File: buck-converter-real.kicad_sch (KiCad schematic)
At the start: 118 parts, among them J1 USB_C_2.0_16P, J10 I2C1, J14 Conn_01x04, J15 Conn_01x06, J2 U.FL, J3 MSD-1-A, J4 POWER, J7 Conn_01x06 2.54mm Screw Termi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, J8 I2C1, J9 SWD, Q10 NTTFS5C680NL, Q8 DMT6030LFCL-7, Q9 NTTFS5C680NL, SW1 WIO_RST, SW2 SW, SW3 SW, U1 MIC4605, U10 TLV75733PDRV 3V3@1A, U11 TPS613222ADBV, U12 INA180A1, U13 TPS22991CRAAR, U2 LM66200DRLR, U4 LV2862XDDC, U6 TPT482-VS2R, U7 TPS22991CRAAR, U8 LM66200DRLR, Y2 Crystal_GND2

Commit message: All routed
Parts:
- removed D13: E1J, Diode_SMD:D_SOD-123F, symbol PCM_Diode_Schottky_AKL:SS56
- removed Q8: DMT6030LFCL-7, buck-forest:DMT6030LFCL-7, symbol buck-wio:DMT6030LFCL-7

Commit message: Swap clamp diode to lower voltage.
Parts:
- added R52, R53: 1M, Resistor_SMD:R_0603_1608Metric_Pad0.98x0.95mm_HandSolder, symbol Device:R_US
- D4: value SMBJ54A -> SMBJ36A
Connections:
- net GND: now also R52.2, R53.2
- net at R47.2, U1.8 (LO): now also R53.1
- net at R48.2, U1.3 (HO): now also R52.1

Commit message: Add details to schematic
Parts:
- TP2: footprint (none) -> TestPoint:TestPoint_Keystone_5015_Micro_Mini
- U1: value MIC4605 -> MIC4605-2YM
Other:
- note added: "3V3 ~10mA MAX"
- note added: "3V3 ~160mA MAX"
- note added: "3V3 ~600mA budget"
- note added: "@ ~200mAnom load"
- note added: "USB Interface (Device/Host)"
- note added: "WIO I2C"
- note removed: "@ 400 mAnom"
- note removed: "USB Interface"
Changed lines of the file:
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@@
 	(text "Ideal diode (OR)"
 		(exclude_from_sim no)
-		(at 216.662 221.234 0)
+		(at 215.9 218.694 0)
 		(effects
 			(font
@@
 	(text "USB"
 		(exclude_from_sim no)
-		(at 131.826 281.686 0)
+		(at 132.588 285.75 0)
 		(effects
 			(font
@@
 		)
 	)
+	(text "3V3 ~600mA budget"
+		(exclude_from_sim no)
+		(at 676.656 314.96 0)
+		(effects
+			(font
+				(size 1.27 1.27)
+			)
+		)
+	)
 	(text "USB 5V out switch"
 		(exclude_from_sim no)
@@
 		)
 	)
-	(text "USB Interface"
+	(text "USB Interface\n(Device/Host)"
 		(exclude_from_sim no)
 		(at 360.934 279.654 0)
@@
 		)
 	)
+	(text "3V3 ~10mA MAX"
+		(exclude_from_sim no)
+		(at 625.348 169.418 0)
+		(effects
+			(font
+				(size 1.27 1.27)
+			)
+		)
+	)
+	(text "WIO I2C"
+		(exclude_from_sim no)
+		(at 676.656 311.658 0)
+		(effects
+			(font
+				(size 2.54 2.54)
+				(thickness 0.508)
+				(bold yes)
+			)
+		)
+	)
 	(text "Active Low"
 		(exclude_from_sim no)
@@
 		)
 	)
+	(text "3V3 ~160mA MAX"
+		(exclude_from_sim no)
+		(at 546.608 218.948 0)
+		(effects
+			(font
+				(size 1.27 1.27)
+			)
+		)
+	)
 	(text "WIO SWD"
 		(exclude_from_sim no)
@@
 		)
 	)
-	(text "@ 400 mAnom"
+	(text "@ ~200mAnom load"
 		(exclude_from_sim no)
-		(at 182.118 168.148 0)
+		(at 173.736 165.1 0)
 		(effects
 			(font
@@
 		(dnp no)
 		(property "Reference" "J1"
-			(at 126.492 301.498 0)
+			(at 130.81 301.498 0)
 			(show_name no)
 			(do_not_autoplace no)
@@
 		)
 		(property "Value" "USB_C_2.0_16P"
-			(at 126.492 304.038 0)
+			(at 130.81 304.038 0)
 			(show_name no)
 			(do_not_autoplace no)
@@
 		(dnp no)
 		(property "Reference" "U13"
-			(at 42.926 233.172 0)
+			(at 43.18 230.886 0)
 			(show_name no)
 			(do_not_autoplace no)
@@
 		)
 		(property "Value" "TPS22991CRAAR"
-			(at 42.926 235.712 0)
+			(at 43.18 233.426 0)
 			(show_name no)
 			(do_not_autoplace no)
@@
 			)
 		)
-		(property "Description" ""
-			(at 43.18 243.84 0)
-			(hide yes)
+		(property "Description" "2A Max Cont."
+			(at 43.434 235.458 0)
 			(show_name no)
 			(do_not_autoplace no)
@@
 			)
 		)
-		(property "Footprint" ""
+		(property "Footprint" "TestPoint:TestPoint_Keystone_5015_Micro_Mini"
 			(at 182.88 208.28 0)
 			(hide yes)
@@
 		(dnp no)
 		(property "Reference" "U2"
-			(at 215.9 226.06 0)
+			(at 215.9 223.266 0)
 			(show_name no)
 			(do_not_autoplace no)
@@
 		)
 		(property "Value" "LM66200DRLR"
-			(at 215.9 228.346 0)
+			(at 215.9 225.552 0)
 			(show_name no)
 			(do_not_autoplace no)
@@
 			)
 		)
-		(property "Description" ""
-			(at 215.9 238.76 0)
-			(hide yes)
+		(property "Description" "2.5A Cont."
+			(at 215.9 227.584 0)
 			(show_name no)
 			(do_not_autoplace no)
@@
 		(dnp no)
 		(property "Reference" "U7"
-			(at 182.626 253.492 0)
+			(at 182.88 251.206 0)
 			(show_name no)
 			(do_not_autoplace no)
@@
 		)
 		(property "Value" "TPS22991CRAAR"
-			(at 182.626 256.032 0)
+			(at 182.88 253.746 0)
 			(show_name no)
 			(do_not_autoplace no)
@@
 			)
 		)
-		(property "Description" ""
-			(at 182.88 264.16 0)
-			(hide yes)
+		(property "Description" "2A Max Cont."
+			(at 182.88 256.286 0)
 			(show_name no)
 			(do_not_autoplace no)
@@
 		(in_pos_files yes)
 		(dnp no)
-		(fields_autoplaced yes)
 		(property "Reference" "U1"
-			(at 284.2795 111.76 0)
+			(at 272.288 111.252 0)
 			(show_name no)
 			(do_not_autoplace no)
@@
 			)
 		)
-		(property "Value" "MIC4605"
-			(at 284.2795 114.3 0)
+		(property "Value" "MIC4605-2YM"
+			(at 267.208 114.046 0)
 			(show_name no)
 			(do_not_autoplace no)

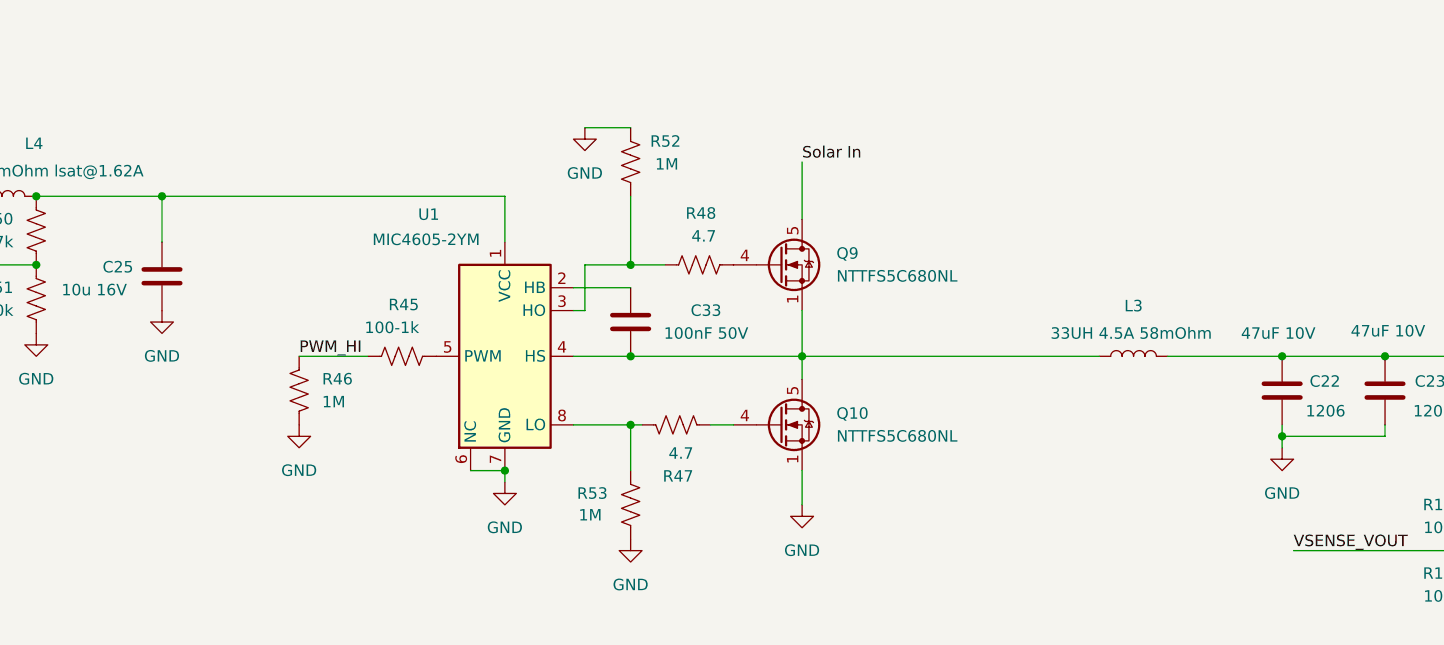
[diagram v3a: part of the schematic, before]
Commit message: Add test point footprint and pads.
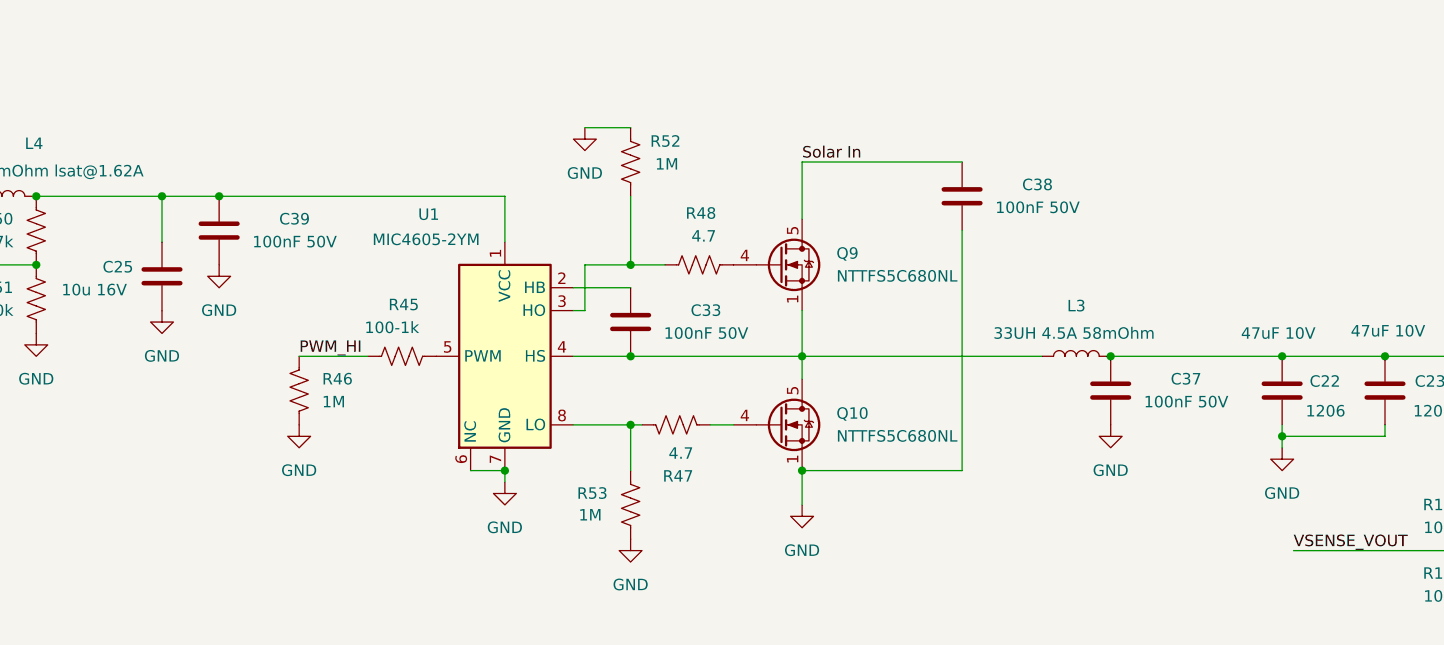
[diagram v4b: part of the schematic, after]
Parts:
- added C37, C38, C39: 100nF 50V, Capacitor_SMD:C_0603_1608Metric_Pad1.08x0.95mm_HandSolder, symbol PCM_Capacitor_AKL:C_0805
- TP1: footprint (none) -> buck-forest:Testpad
- TP2: footprint TestPoint:TestPoint_Keystone_5015_Micro_Mini -> buck-forest:Testpad
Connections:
- net GND: now also C37.1, C38.1, C39.1
- net Solar In: now also C38.2
- net at C25.1, L4.2, R50.1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: now also C39.2
- net at C22.1, C23.1, F1.1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: now also C37.2
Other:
- moved on the sheet: L3

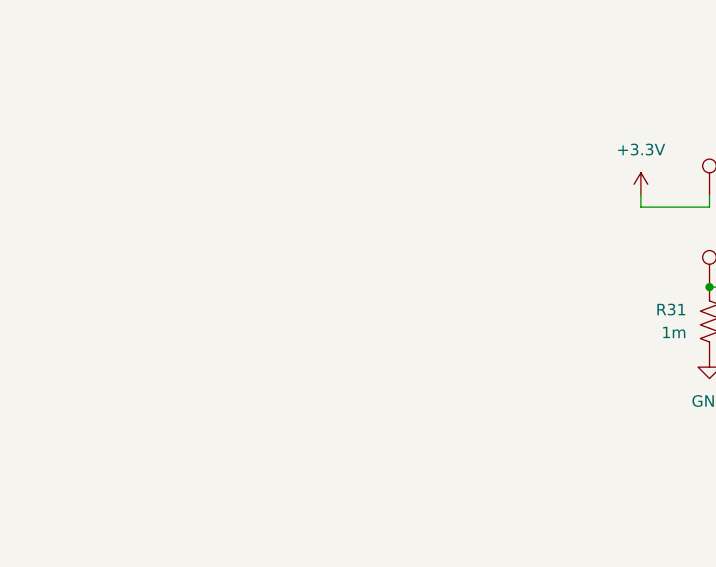
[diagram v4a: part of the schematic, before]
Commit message: Add test holes. More to come
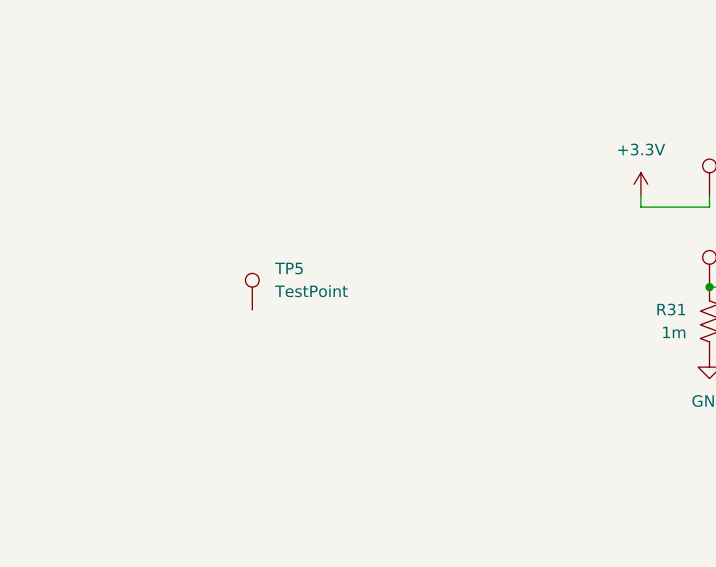
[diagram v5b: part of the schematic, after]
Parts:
- added TP5: TestPoint, buck-forest:Testhole, symbol Connector:TestPoint
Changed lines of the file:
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@@
+	)
+	(symbol
+		(lib_id "Connector:TestPoint")
+		(at 39.37 172.72 0)
+		(unit 1)
+		(body_style 1)
+		(exclude_from_sim no)
+		(in_bom yes)
+		(on_board yes)
+		(in_pos_files yes)
+		(dnp no)
+		(fields_autoplaced yes)
+		(property "Reference" "TP5"
+			(at 41.91 168.1479 0)
+			(show_name no)
+			(do_not_autoplace no)
+			(effects
+				(font
+					(size 1.27 1.27)
+				)
+				(justify left)
+			)
+		)
+		(property "Value" "TestPoint"
+			(at 41.91 170.6879 0)
+			(show_name no)
+			(do_not_autoplace no)
+			(effects
+				(font
+					(size 1.27 1.27)
+				)
+				(justify left)
+			)
+		)
+		(property "Footprint" "buck-forest:Testhole"
+			(at 44.45 172.72 0)
+			(hide yes)
+			(show_name no)
+			(do_not_autoplace no)
+			(effects
+				(font
+					(size 1.27 1.27)
+				)
+			)
+		)
+		(property "Datasheet" ""
+			(at 44.45 172.72 0)
+			(hide yes)
+			(show_name no)
+			(do_not_autoplace no)
+			(effects
+				(font
+					(size 1.27 1.27)
+				)
+			)
+		)
+		(property "Description" "test point"
+			(at 39.37 172.72 0)
+			(hide yes)
+			(show_name no)
+			(do_not_autoplace no)
+			(effects
+				(font
+					(size 1.27 1.27)
+				)
+			)
+		)
+		(pin "1"
+		)
+		(instances
+			(project "buck-converter-real"
+				(path "/cbc98a1b-0533-4e8d-81af-0515d3e50555"
+					(reference "TP5")
+					(unit 1)
+				)
+			)
+		)
 	)
 	(symbol

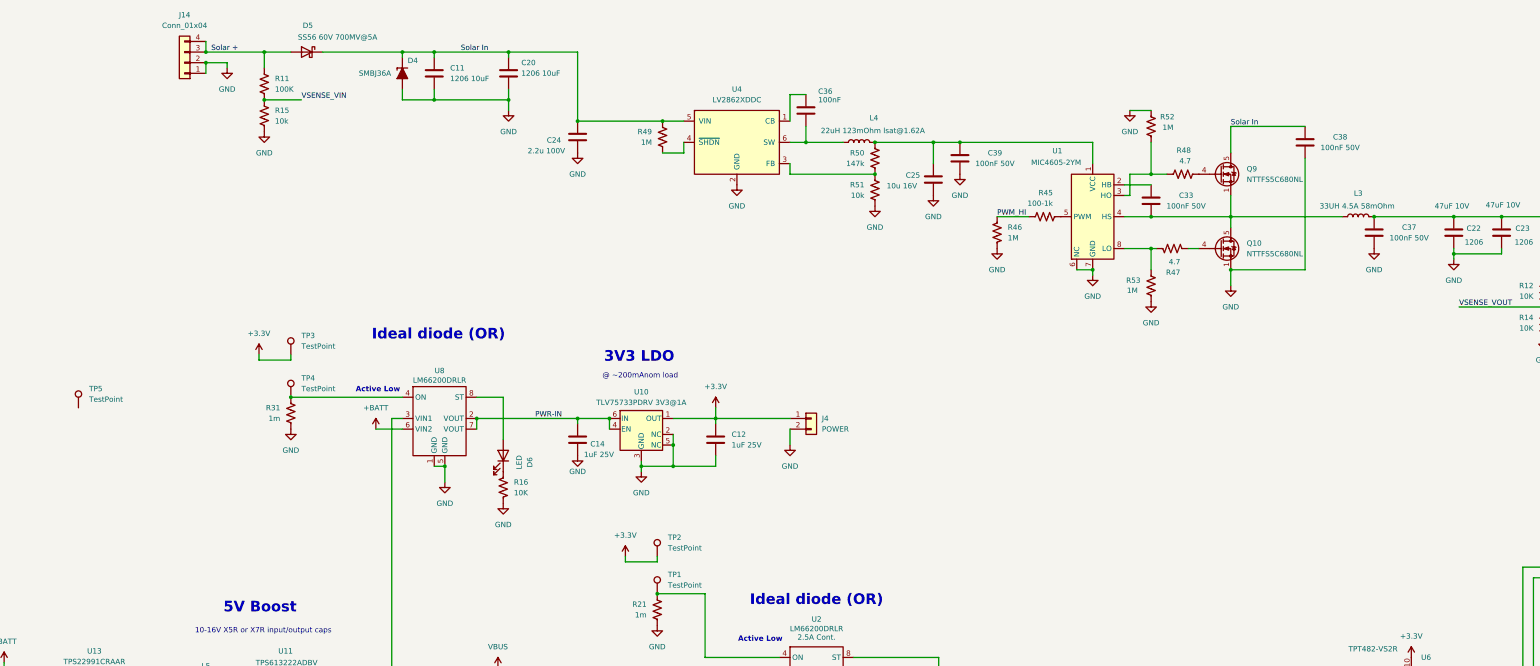
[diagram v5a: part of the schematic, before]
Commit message: Add more test holes.
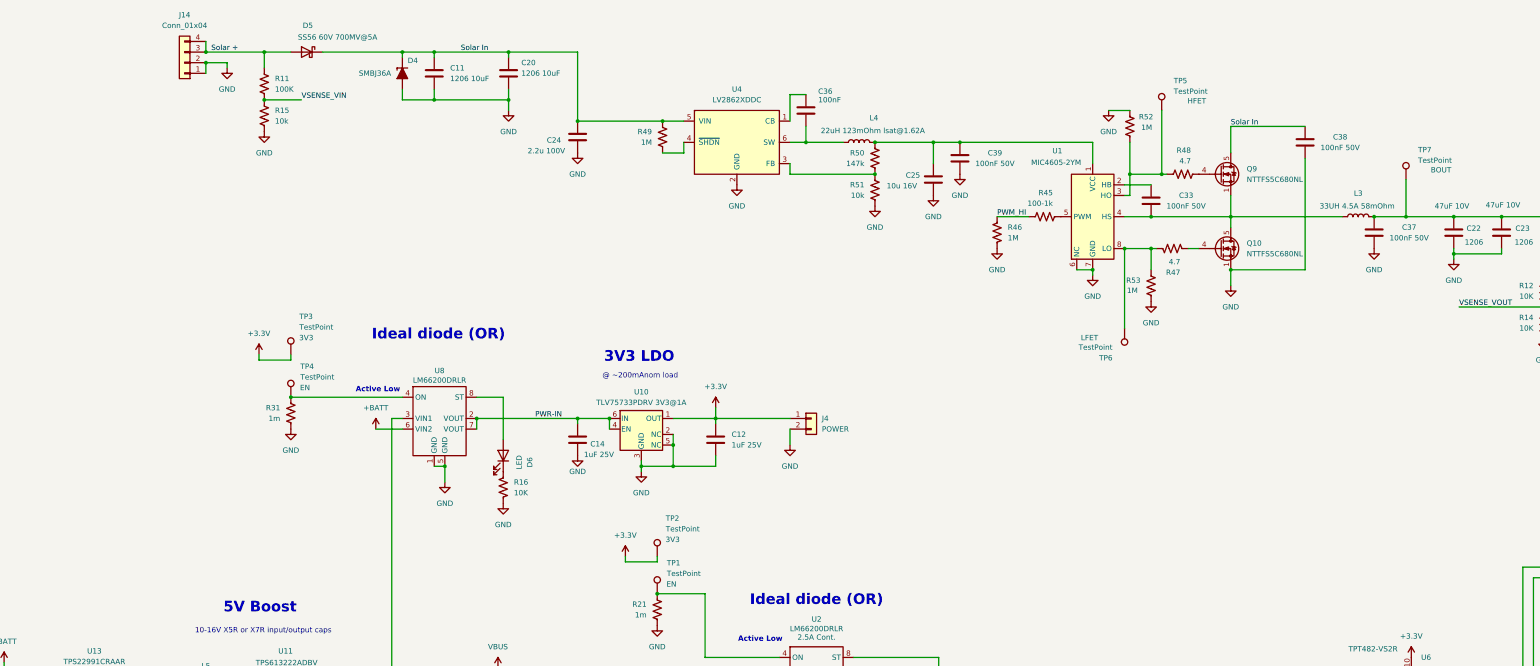
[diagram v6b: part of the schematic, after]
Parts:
- added TP6, TP7: TestPoint, buck-forest:Testhole-1.00mm, symbol Connector:TestPoint
- TP1, TP2: footprint buck-forest:Testpad -> buck-forest:Testhole-1.00mm
- TP3, TP4: footprint (none) -> buck-forest:Testhole-1.00mm
- TP5: footprint buck-forest:Testhole -> buck-forest:Testhole-1.00mm
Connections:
- net at R47.2, R53.1, U1.8 (LO): now also TP6.1
- net at C22.1, C23.1, C37.2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: now also TP7.1
- net at TP5.1: now also R48.2, R52.1, U1.3 (HO)
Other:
- moved on the sheet: R52, TP5

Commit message: Route crystal.
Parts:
- removed SW3: SW, Button_Switch_SMD:SW_SPST_PTS647_Sx38, symbol Switch:SW_Omron_B3FS
- removed TP7: TestPoint, buck-forest:Testhole-1.00mm, symbol Connector:TestPoint
- added D13: LED, LED_SMD:LED_0603_1608Metric_Pad1.05x0.95mm_HandSolder, symbol Device:LED
- added TP8: TestPoint, buck-forest:Testhole-1.00mm, symbol Connector:TestPoint
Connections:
- net +3.3V: now also R41.2; no longer R41.1
- net at U9.18 (PA11): now also D13.1 (K)
- net at R45.1, U1.5 (PWM): now also TP8.1
- new net: D13.2 (A), R41.1

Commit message: Add gpio
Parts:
- removed D13: LED, LED_SMD:LED_0603_1608Metric_Pad1.05x0.95mm_HandSolder, symbol Device:LED
- removed R41: 10K, Resistor_SMD:R_0603_1608Metric_Pad0.98x0.95mm_HandSolder, symbol Device:R_US
- added C40: 10uF 100V, Capacitor_SMD:C_0603_1608Metric_Pad1.08x0.95mm_HandSolder, symbol PCM_Capacitor_AKL:C_0805
- added J5: Conn_01x02, Connector_PinHeader_1.00mm:PinHeader_1x02_P1.00mm_Vertical, symbol Connector_Generic:Conn_01x02
- C38: value 100nF 50V -> 100nF 100V
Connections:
- net GND: now also C40.1, J5.2 (Pin_2)
- net Solar In: now also C40.2
- net at U9.18 (PA11): now also J5.1 (Pin_1)
